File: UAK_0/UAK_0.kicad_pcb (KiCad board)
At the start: 2 copper layers, 100 x 90 mm, 79 parts, among them K1 Кнопка_FSMSM, K2 Кнопка_FSMSM, X1 Крепежное_отверстие_М3, X2 Крепежное_отверстие_М3, X3 Крепежное_отверстие_М3, X4 Крепежное_отверстие_М3, X5 Крепежное_отверстие_d2, X6 Крепежное_отверстие_d2, X7 Крепежное_отверстие_d2

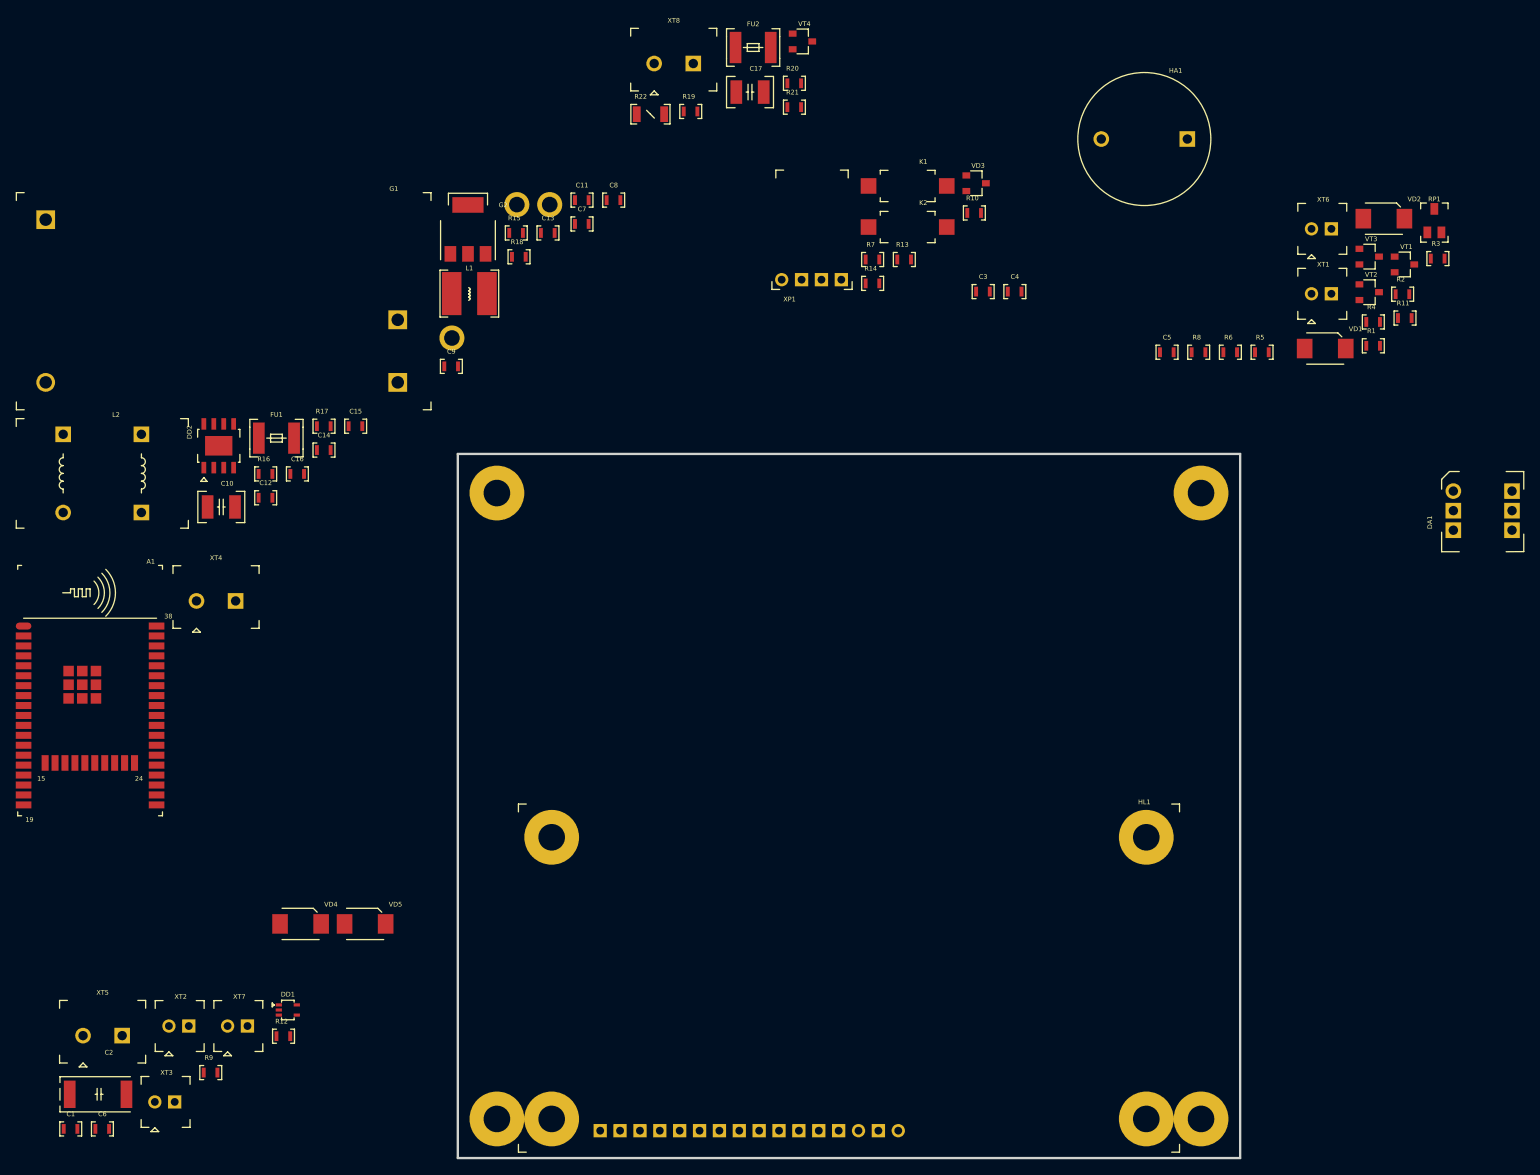
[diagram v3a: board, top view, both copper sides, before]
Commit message: есть трассировка питания
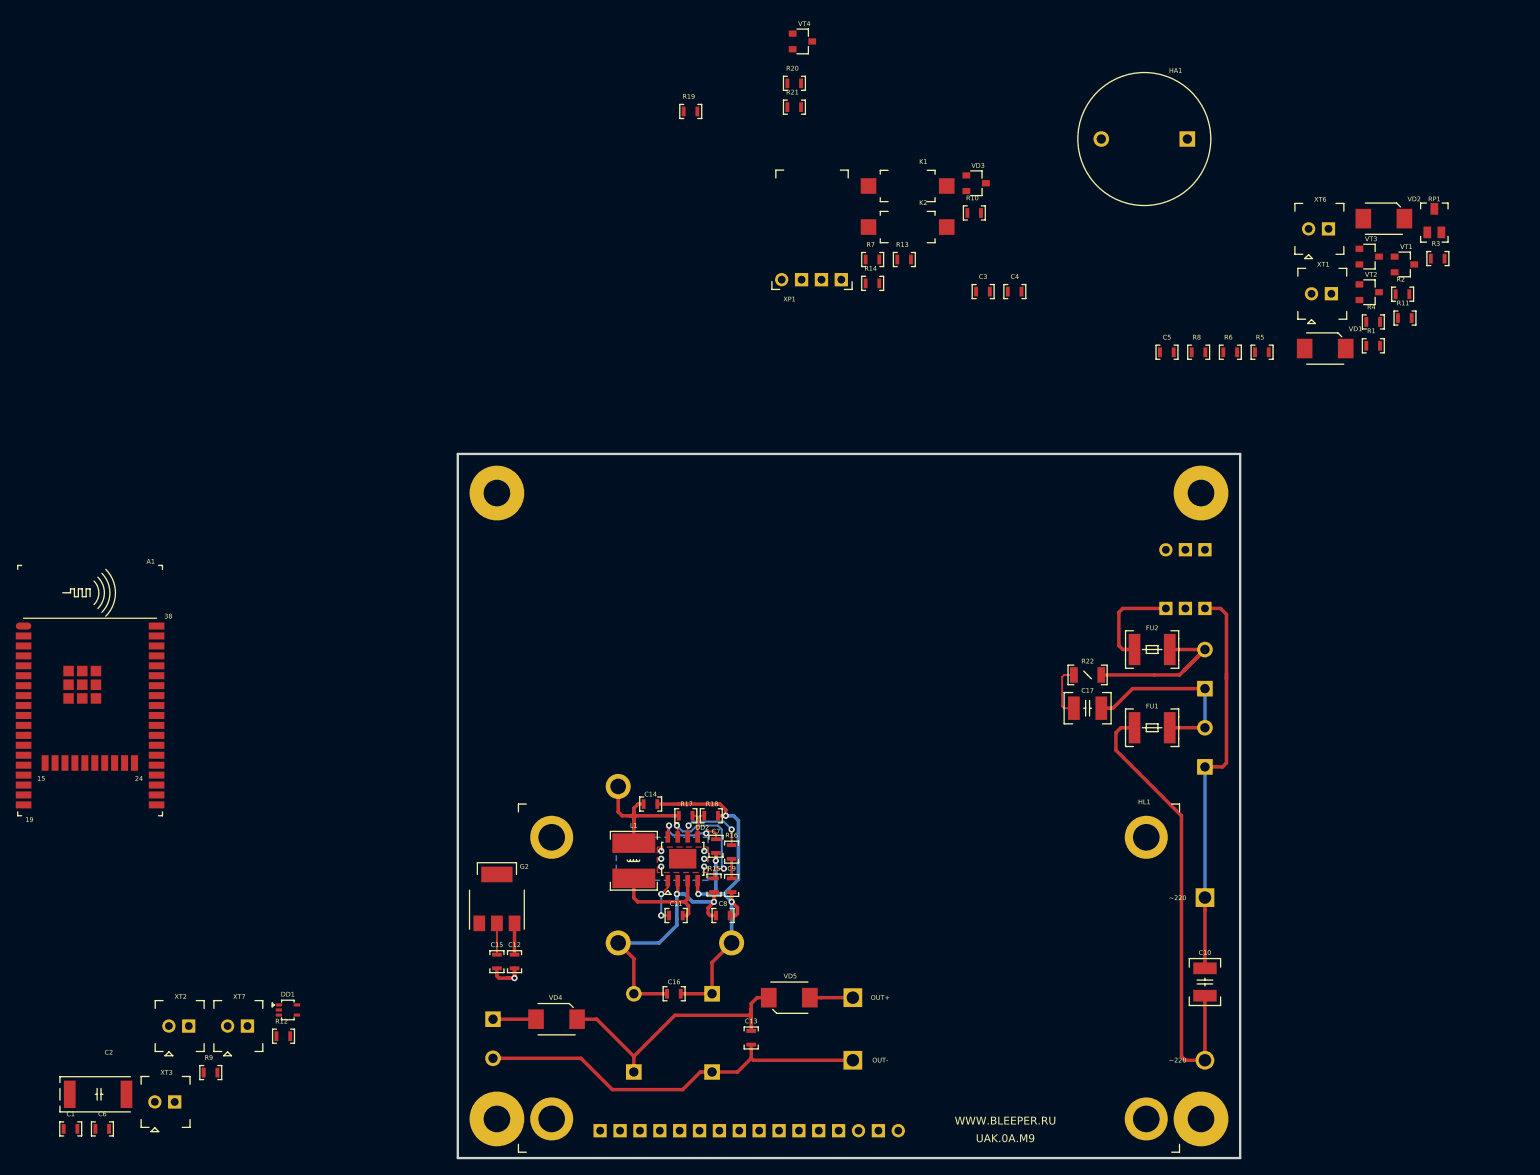
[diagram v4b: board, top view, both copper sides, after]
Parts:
- DA1, G1, L2, X5, X6, X7, XT4, XT5, XT8: moved to B.Cu
- moved G1 171.6 mm to (170.5, 127.5), turned to 180 degrees
- moved C10 142.0 mm to (170.5, 119.2), turned to 90 degrees
- moved XT4 129.9 mm to (170.5, 85.0), turned to 270 degrees
- moved FU1 122.2 mm to (166.0, 85.0), turned to 180 degrees
- moved C13 105.5 mm to (112.5, 123.8), turned to 270 degrees
- moved XT8 102.8 mm to (170.5, 75.0), turned to 270 degrees
- moved X6 97.2 mm to (110.0, 112.5), turned to 270 degrees
- moved L2 95.4 mm to (97.5, 119.0)
- moved R22 93.1 mm to (157.2, 78.2), turned to 180 degrees
- moved C8 92.5 mm to (108.0, 109.0)
- moved FU2 92.3 mm to (161.5, 75.0)
- moved C11 92.2 mm to (102.0, 109.0)
- moved C17 89.8 mm to (153.8, 82.5)
- moved R15 88.2 mm to (107.8, 106.0), turned to 90 degrees
- moved G2 85.6 mm to (80.0, 106.2)
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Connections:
- net /BUTT_2 renamed /GND
- net Net-(C10-Pad1) renamed /SUPPLY_POWER/220_L_FU
- net Net-(C11-Pad2) renamed /SUPPLY_POWER/5V_DC-DC
- net Net-(C13-Pad1) renamed /SUPPLY_POWER/12V_NOISE
- net Net-(G1-Pad+V) renamed /SUPPLY_POWER/12V_OUT_G
- C17 pad 2: /220_N_OUT -> /220_L
- DA1 pad 1: /220_N_OUT -> Net-(DA1-Pad1)
- DA1 pad 4: (no net) -> /220_N
- DA1 pad 5: (no net) -> Net-(DA1-Pad5)
- DA1 pad 6: (no net) -> /220_N_FU
- FU2 pad 1: Net-(DA1-Pad3) -> /220_N_FU
- FU2 pad 2: /220_N -> /220_N_OUT
- R22 pad 1: /220_L -> /220_N_OUT
- XT5 pad 1: /12V_RES -> /0V_RES
- XT5 pad 2: /0V_RES -> /12V_RES
- XT8 pad 1: /220_L -> /220_N_OUT
- XT8 pad 2: /220_N_OUT -> /220_L
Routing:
- net /GND: track 0.00 -> 62.3 mm, vias 0 -> 5
- net /SUPPLY_POWER/220_L_FU: track 0.00 -> 58.9 mm
- net /220_N: track 0.00 -> 51.5 mm
- net /0V_RES: track 0.00 -> 51.2 mm
- net /SUPPLY_POWER/12V_NOISE: track 0.00 -> 35.4 mm
- net /12V: track 0.00 -> 35.1 mm, vias 0 -> 2
- net /5V: track 0.00 -> 23.8 mm
- net /220_L: track 0.00 -> 23.8 mm
- net /220_N_OUT: track 0.00 -> 23.0 mm
- net Net-(DD2-Pad7): track 0.00 -> 15.5 mm, vias 0 -> 2
- net /SUPPLY_POWER/5V_DC-DC: track 0.00 -> 14.6 mm
- net /220_N_FU: track 0.00 -> 12.7 mm
- net Net-(DD2-Pad6): track 0.00 -> 9.62 mm, vias 0 -> 2
- net Net-(C7-Pad1): track 0.00 -> 9.54 mm, vias 0 -> 2
- net Net-(C17-Pad1): track 0.00 -> 6.96 mm
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- added copper zone on B.Cu, net BOTTOM
- added copper zone on F.Cu, net BOTTOM
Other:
- net class PWR_1A added: clearance 0.25, trace_width 0.45, via_dia 0.8, via_drill 0.4
- net class PWR_220 added: clearance 0.8, trace_width 0.45, via_dia 0.8, via_drill 0.4
- board text added: "UAK.0A.M9"
- board text added: "WWW.BLEEPER.RU"

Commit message: начата установка ESP32
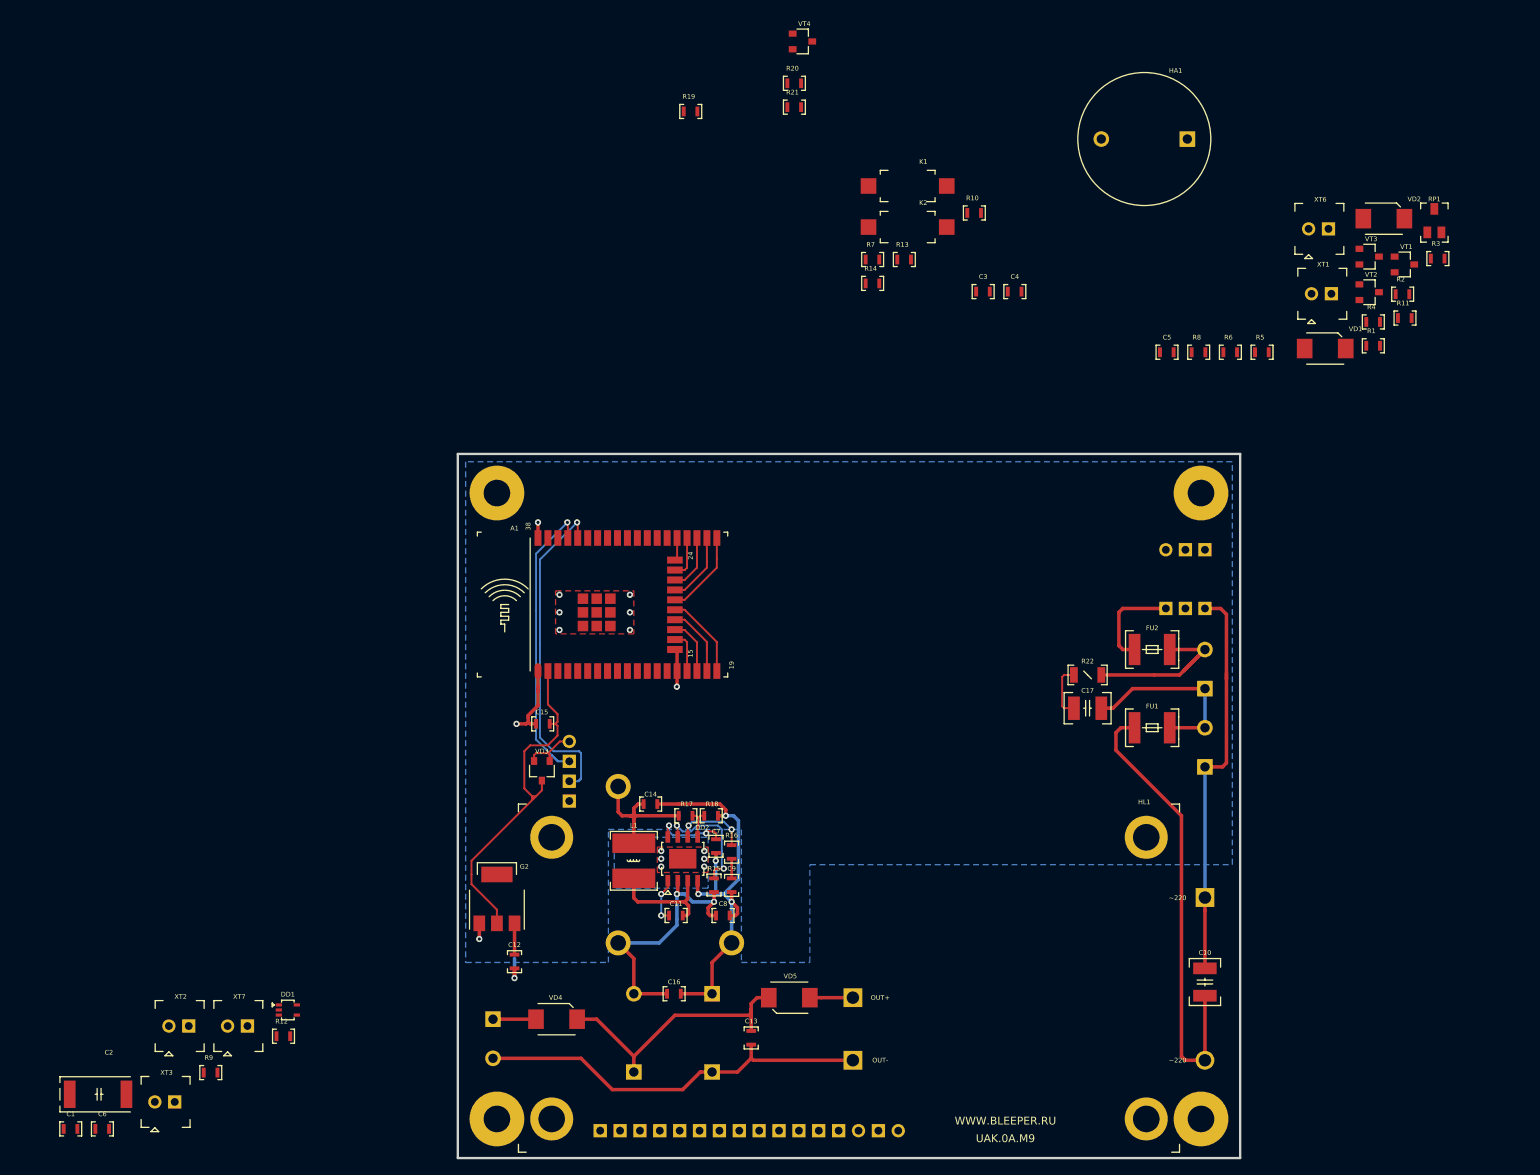
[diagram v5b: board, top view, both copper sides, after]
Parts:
- XP1: moved to B.Cu
- moved VD3 93.4 mm to (85.8, 90.5), turned to 270 degrees
- moved A1 66.0 mm to (85.2, 77.8), turned to 90 degrees
- moved XP1 65.0 mm to (89.2, 86.8), turned to 270 degrees
- moved C15 30.3 mm to (86.8, 84.5), turned to 180 degrees
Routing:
- net /BOOT_UART_RX: track 0.00 -> 42.8 mm, vias 0 -> 1
- net /3V3: track 4.00 -> 45.6 mm
- net /BOOT_UART_TX: track 0.00 -> 37.9 mm, vias 0 -> 1
- net /GND: track 62.3 -> 79.5 mm, vias 5 -> 15
- net Net-(A1-Pad20): track 0.00 -> 10.9 mm
- net Net-(A1-Pad19): track 0.00 -> 10.8 mm
- net Net-(A1-Pad18): track 0.00 -> 10.1 mm
- net Net-(A1-Pad21): track 0.00 -> 9.06 mm
- net Net-(VD3-Pad1): track 0.00 -> 7.81 mm
- net Net-(A1-Pad22): track 0.00 -> 7.26 mm
- net Net-(A1-Pad17): track 0.00 -> 7.15 mm
- net /LCD_A0: track 0.00 -> 5.71 mm
- net /LCD_LED: track 0.00 -> 5.37 mm
- net /LCD_E: track 0.00 -> 2.87 mm
- added copper zone on B.Cu, net /GND
- added copper zone on F.Cu, net /GND

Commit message: закончена трассировка, обновлена PDF и PNG, добавлен STEP
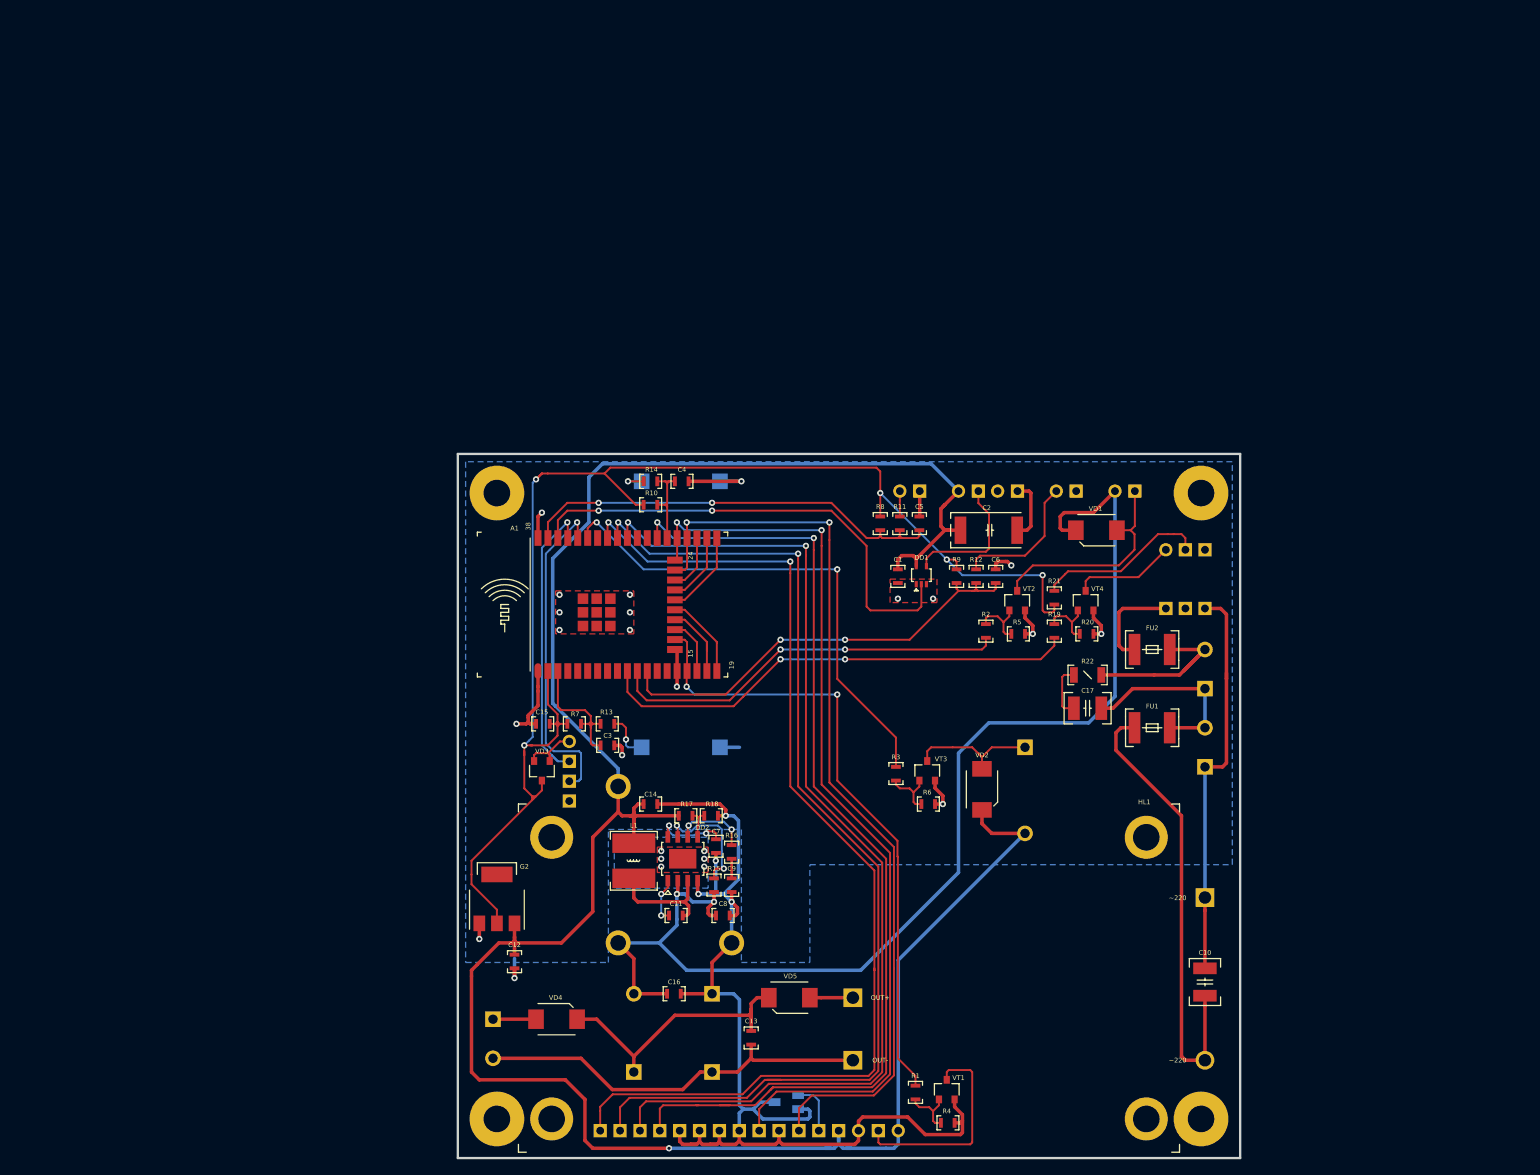
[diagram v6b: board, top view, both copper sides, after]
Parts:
- added D1: NI, N_ICO:ni_10x10, B.Cu at (79.4, 107.2)
- added D2: QR, N_ICO:El-nikitos_QR_10x10, B.Cu at (89.2, 106.8)
- HA1, K1, K2, RP1, XT1, XT2, XT3, XT6, XT7: moved to B.Cu
- moved RP1 139.8 mm to (117.0, 132.8), turned to 270 degrees
- moved C6 135.5 mm to (143.8, 64.8), turned to 270 degrees
- moved C2 134.8 mm to (139.2, 59.8)
- moved XT3 133.0 mm to (144.0, 54.8)
- moved C1 128.4 mm to (131.2, 64.8), turned to 270 degrees
- moved XT7 126.1 mm to (151.5, 54.8)
- moved XT2 121.9 mm to (139.0, 54.8)
- moved VT1 120.6 mm to (137.5, 131.2), turned to 90 degrees
- moved R4 115.9 mm to (136.8, 135.5)
- moved R9 115.7 mm to (138.8, 64.8), turned to 270 degrees
- moved R1 112.2 mm to (133.5, 132.5), turned to 90 degrees
- moved R12 107.5 mm to (141.2, 64.8), turned to 270 degrees
- moved DD1 98.2 mm to (134.2, 65.5), turned to 90 degrees
- moved R3 95.5 mm to (131.0, 91.8), turned to 90 degrees
- moved VT3 86.7 mm to (135.0, 90.5), turned to 90 degrees
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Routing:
- net /5V: track 23.8 -> 305.4 mm, vias 0 -> 1
- net /LCD_DATA_7: track 0.00 -> 137.1 mm, vias 0 -> 2
- net /LCD_DATA_6: track 0.00 -> 136.7 mm, vias 0 -> 2
- net /GND: track 79.5 -> 214.2 mm, vias 15 -> 23
- net /LCD_DATA_5: track 0.00 -> 133.1 mm, vias 0 -> 2
- net /LCD_DATA_4: track 0.00 -> 130.5 mm, vias 0 -> 2
- net /3V3: track 45.6 -> 175.9 mm, vias 0 -> 5
- net /12V: track 35.1 -> 156.4 mm
- net /LCD_E: track 2.87 -> 118.3 mm, vias 0 -> 2
- net /LCD_A0: track 5.71 -> 116.8 mm, vias 0 -> 2
- net /LCD_LED: track 5.37 -> 81.2 mm, vias 0 -> 2
- net /BUZZER: track 0.00 -> 64.3 mm, vias 0 -> 2
- net /MC_220_OUT: track 0.00 -> 62.2 mm, vias 0 -> 2
- net /LED_WS2812: track 0.00 -> 62.1 mm, vias 0 -> 2
- net /EXT_BUTTON: track 0.00 -> 56.4 mm, vias 0 -> 2
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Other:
- board text added: "12V"
- board text added: "12V OUT"
- board text added: "220_L IN"
- board text added: "220_L OUT"
- board text added: "220_N IN"
- board text added: "220_N RELAY"
- board text added: "3V3 IN"
- board text added: "5V"
- board text added: "5V OUT"
- board text added: "BOOT"
- board text added: "BUTT_LED"
- board text added: "DOOR"
- board text added: "EXT_0V IN"
- board text added: "EXT_12V IN"
- board text added: "EXT_BUTTON"
- board text added: "GND"
- board text added: "LED_WS2812"
- board text added: "RESET"
- board text added: "RX"
- board text added: "TX"
- board text added: "UAK.0B.M9"
- board text removed: "UAK.0A.M9"

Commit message: UAK_0C. Убрал лого Ni, добавлены gerber
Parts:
- removed D1: NI, N_ICO:ni_10x10
- removed D2: QR, N_ICO:El-nikitos_QR_10x10
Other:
- board text added: "UAK.0C.M9"
- board text removed: "UAK.0B.M9"
